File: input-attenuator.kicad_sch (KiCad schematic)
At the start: 44 parts, among them J1 DC_INTF, J2 RF_IN, J3 RX_1_RF, J4 RX_2_RF, K1 EE2-5TNU-L, K2 EE2-5TNU-L, K3 EE2-5TNU-L, K4 EE2-5TNU-L, Q1 MMBT3904, Q2 MMBT3904, Q3 MMBT3904, Q4 MMBT3904, Q5 MMBT3904, Q6 MMBT3904, Q7 MMBT3904, Q8 MMBT3904, U1 74HC595

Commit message: noComment
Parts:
- added C? (x4): 0.22u, Capacitor_SMD:C_0805_2012Metric, symbol Device:C_Small
- added C?: 100u, Capacitor_SMD:CP_Elec_6.3x5.4_Nichicon, symbol Device:CP_Small
- added D? (x6): 1N4148WS, Diode_SMD:D_SOD-323, symbol Device:D_Small_ALT
- added J?: DC_INTF, Connector_PinHeader_2.54mm:PinHeader_1x06_P2.54mm_Vertical, symbol Connector:Conn_01x06_Male
- added K? (x3): EE2-5TNU-L, Relay_SMD:Relay_DPDT_Kemet_EE2_NU_DoubleCoil, symbol Relay:EE2-5TNU
- added Q? (x8): BC858, Package_TO_SOT_SMD:SOT-23, symbol Transistor_BJT:BC858
- added R22, R23, R24, R? (x6): _, Resistor_SMD:R_0805_2012Metric, symbol Device:R_Small_US
- added R? (x7): 22K, Resistor_SMD:R_0805_2012Metric, symbol Device:R_Small_US
- added R? (x4): 1M, Resistor_SMD:R_0805_2012Metric, symbol Device:R_Small_US
- added R? (x2): 82.2, Resistor_SMD:R_0805_2012Metric, symbol Device:R_Small_US
- added R? (x4): 14.0_, Resistor_SMD:R_0805_2012Metric, symbol Device:R_Small_US
- added U1 (x4), U? (x16): 74HC00, symbol 74xx:74HC00
- R2, R3: value 14.0 -> 14.0_
- R4: value 82.2 -> 82.2
- renumbered U1 to U?
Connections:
- net A1_OFF: no longer R5.1
- net A1_ON: no longer R1.1
- net A2_ON: no longer R6.1
- net GND: now also D1.2 (A), D2.2 (A), K1.1, K1.6, C?.2, C?.2, C?.2, C?.2, C?.2, D?.2 (A), D?.2 (A), D?.2 (A), D?.2 (A), D?.2 (A), D?.2 (A), J?.2 (Pin_2), K?.1, K?.1, K?.1, K?.6, K?.6, K?.6, R24.2, R?.1, R?.2, R?.2, R?.2, R?.2; no longer Q1.2 (E), Q2.2 (E)
- net RF_IN: now also K?.4, K?.4
- net RX_2_RF: no longer J4.1 (In)
- net VRelay: now also C?.1, J?.1 (Pin_1), Q?.2 (E), Q?.2 (E), Q?.2 (E), Q?.2 (E), Q?.2 (E), Q?.2 (E), Q?.2 (E), Q?.2 (E); no longer D1.1 (K), D2.1 (K), D8.1 (K), K1.1, K1.6, K4.6
- net at K1.5, R3.1: now also R23.1
- net at K1.8, R2.2: now also R22.1
- net at K1.9: now also K?.4; no longer K2.4
- net at Q1.1 (B): no longer R1.2
- net at R5.2: now also Q?.1 (B); no longer Q2.1 (B)
- net at R2.1, R3.2, R4.1: now also R22.2, R23.2, R24.1
- net at K4.3, K4.8: no longer K3.9
- new net: D2.1 (K), K1.12, Q?.3 (C)
- new net: D1.1 (K), K1.7, Q?.3 (C)
- new net: R1.1, U1.3
- new net: Q?.1 (B), R1.2
- new net: R5.1, U1.3
- new net: D8.1 (K), K4.6
- new net: R?.1, U?.3 (x6)
- new net: Q?.1 (B), R?.2 (x6)
- new net: D?.1 (K), K?.7, Q?.3 (C) (x3)
- new net: R?.1, U1.1, U1.1, U1.2, U?.3
- new net: U1.1, U1.3
- new net: C?.1, R?.2, U1.1, U1.2, U1.2
- new net: U?.1, U?.3 (x3)
- new net: C?.1, R?.2, U?.1, U?.2, U?.2 (x3)
- new net: R?.1, U?.1, U?.1, U?.2, U?.3 (x3)
- new net: U?.2, U?.3 (x3)
- new net: K?.5, R?.1, R?.1 (x2)
- new net: R?.1, R?.1, R?.1, R?.2, R?.2, R?.2 (x2)
- new net: D?.1 (K), K?.12, Q?.3 (C) (x3)
- new net: U1.2, U1.3
- new net: K?.10, K?.3 (x2)
- new net: K?.8, R?.1, R?.2 (x2)
- new net 10dB: U?.1
- new net 20dB: U?.1
- new net 5dB: J?.3 (Pin_3), U?.1
- new net Rx: U?.1
- new net powerDown: R?.2, U?.2, U?.2, U?.2, U?.2
- now unconnected: Q1.3 (C), Q2.3 (C)
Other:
- note removed: "Receiver selector"
- moved on the sheet: C1, C2, D1, D2, D3, D4, D5, D6, D7, D8, J1, J2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

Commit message: relays
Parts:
- removed J2: RF_IN, Connector_Coaxial:SMA_Amphenol_132134_Vertical, symbol Connector:Conn_Coaxial
- removed Q? (x3): BC858, Package_TO_SOT_SMD:SOT-23, symbol Transistor_BJT:BC858
- removed R? (x3): 22K, Resistor_SMD:R_0805_2012Metric, symbol Device:R_Small_US
- added J?: RF_IN, Connector_Coaxial:SMA_Amphenol_132134_Vertical, symbol Connector:Conn_Coaxial
- added Q? (x3): BC858, Package_TO_SOT_SMD:SOT-23, symbol Transistor_BJT:BC858
- added R? (x3): 22K, Resistor_SMD:R_0805_2012Metric, symbol Device:R_Small_US
- added unit 5 of U1
- gave numbers to parts that had none: 3
- renumbered R5 to R2, R3 to R4, R23 to R5, R4 to R6, R24 to R7, R2 to R8, R22 to R9
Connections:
- net GND: now also J?.2 (Ext)
- net RX_1_RF: no longer J3.1 (In)
- net VRelay: now also Q?.2 (E), Q?.2 (E), Q?.2 (E)
- net at R1.1: now also U1.8; no longer U1.3
- net at R2.1: now also U1.11; no longer U1.3
- net Antenna: now reaches J4.1 (In)
- net Antenna: now also K?.4, K?.9
- net at R3.1, U1.1, U1.2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: now also U1.9; no longer U1.1
- net at U1.3: now also U1.12; no longer U1.1
- net at U?.3: now also R?.1 (x3)
- net at D?.1 (K), K?.12: now also Q?.3 (C) (x3)
- net RF_RX: now reaches K?.9
- net RF_RX: now also J3.1 (In)
- net RF_TX: now reaches K?.10
- net RF_TX: now also K?.3, J?.1 (In)
- net at K?.8: now also K1.4
- net at K?.9: now also K?.4
- removed net RF_IN: K1.4, K?.4, K?.4
- new net: C?.1, R3.2, U1.13, U1.4, U1.5
- new net: U1.10, U1.6
- new net: Q?.1 (B), R?.2 (x3)
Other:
- moved on the sheet: C?, D1, D2, D?, J3, J4, K1, K?, Q1, Q2, Q?, R1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

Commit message: relaysPlaced
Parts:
- removed C?: 100u, Capacitor_SMD:CP_Elec_6.3x5.4_Nichicon, symbol Device:CP_Small
- removed D3, D4, D5, D6, D7, D8: 1N4148WS, Diode_SMD:D_SOD-323, symbol Device:D_Small_ALT
- removed J?: DC_INTF, Connector_PinHeader_2.54mm:PinHeader_1x06_P2.54mm_Vertical, symbol Connector:Conn_01x06_Male
- removed K2, K3, K4: EE2-5TNU-L, Relay_SMD:Relay_DPDT_Kemet_EE2_NU_DoubleCoil, symbol Relay:EE2-5TNU
- removed Q2, Q3, Q4, Q5, Q6, Q7, Q8: MMBT3904, Package_TO_SOT_SMD:SOT-23, symbol Transistor_BJT:MMBT3904
- removed R10, R11, R15, R16, R17, R6, R?: 22K, Resistor_SMD:R_0805_2012Metric, symbol Device:R_Small_US
- removed R12, R13: 40.9, Resistor_SMD:R_0805_2012Metric, symbol Device:R_Small_US
- removed R14: 10.1, Resistor_SMD:R_0805_2012Metric, symbol Device:R_Small_US
- removed R7, R8: 26.0, Resistor_SMD:R_0805_2012Metric, symbol Device:R_Small_US
- removed R9: 35.1, Resistor_SMD:R_0805_2012Metric, symbol Device:R_Small_US
- added unit 5 of U2
- added unit 5 of U3
- added unit 5 of U4
- added unit 5 of U5
- U1: footprint (none) -> Package_SO:SO-14_3.9x8.65mm_P1.27mm
- U2, U3, U4, U5: renamed from U?; footprint (none) -> Package_SO:SO-14_3.9x8.65mm_P1.27mm
- gave numbers to parts that had none: 42
- renumbered Q1 to Q3
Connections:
- net A1_OFF is gone; now on net 5dB: U6.1 (QB)
- net A1_ON is gone; now on net Rx: U6.15 (QA)
- net A2_OFF is gone; now on net 20dB: U6.3 (QD)
- net A2_ON is gone; now on net 10dB: U6.2 (QC)
- net VRelay is gone; now on net +5V: C1.1, C2.2, J1.1 (Pin_1), Q1.2 (E), Q2.2 (E), Q4.2 (E), Q5.2 (E), Q6.2 (E), Q7.2 (E), Q8.2 (E), Q9.2 (E), U6.10 (~SRCLR), U6.16 (VCC)
- net 10dB: now also U5.9; no longer U5.1
- net 20dB: now also U5.13; no longer U5.1
- net 5dB: now also U5.5; no longer U5.1
- net GND: now also U1.7 (GND), U2.7 (GND), U3.7 (GND), U4.7 (GND), U5.7 (GND)
- net powerDown: now also U5.10, U5.12, U5.4; no longer U5.2, U5.2, U5.2
- net at K1.4, K2.8: now also K2.5
- net at R2.1: now also U1.6; no longer U1.11
- net at R27.1: now also U3.6; no longer U3.3
- net at R3.1, U1.1, U1.2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: now also U5.6; no longer U5.3
- net at U1.3: now also U1.4; no longer U1.12
- net at U2.3: now also U2.4; no longer U2.1
- net at R25.1: now also U2.6; no longer U2.3
- net at R30.1, U3.1, U3.2: now also U3.9, U5.11; no longer U3.1, U5.3
- net at R28.1, U4.1, U4.2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: now also U4.9; no longer U4.1
- net at R26.1: now also U3.8; no longer U3.3
- net at U1.10: now also U1.11; no longer U1.6
- net at R22.1: now also U4.8; no longer U4.3
- net +5V: now reaches U1.14 (VCC)
- net +5V: now also U2.14 (VCC), U3.14 (VCC), U4.14 (VCC), U5.14 (VCC)
- net at R29.1, U2.1, U2.2: now also U2.9, U5.8; no longer U2.1, U5.3
- net at R23.1: now also U4.6; no longer U4.3
- net at R24.1: now also U2.8; no longer U2.3
- net at U3.3: now also U3.4; no longer U3.1
- net at U4.3: now also U4.4; no longer U4.1
- net A3_OFF: no longer names the net of U6.5 (QF)
- net A3_ON: no longer names the net of U6.4 (QE)
- net RX_1_ON: no longer names the net of U6.6 (QG)
- net RX_2_ON: no longer names the net of U6.7 (QH)
- new net: C4.1, R3.2, U1.12, U1.13, U1.5
- new net: C5.1, R29.2, U2.12, U2.13, U2.5
- new net: C6.1, R30.2, U3.12, U3.13, U3.5
- new net: U3.10, U3.11
- new net: U4.10, U4.11
- new net: U2.10, U2.11
- new net: C3.1, R28.2, U4.12, U4.13, U4.5
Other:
- note removed: "Keep DRC happy"
- moved on the sheet: C1, C2, J1, Q3, U1E, U6

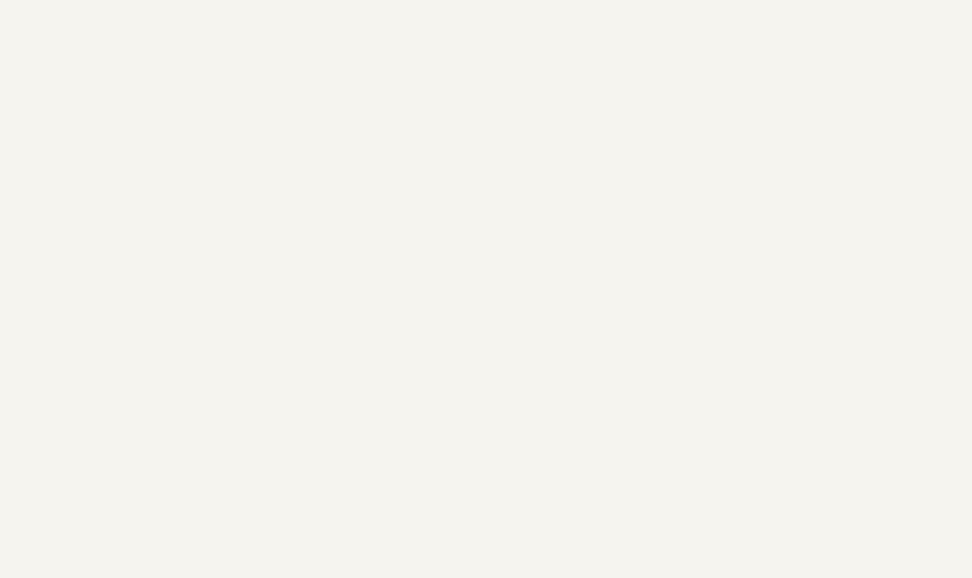
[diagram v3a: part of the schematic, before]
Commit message: Added regulator symbol to custom lib
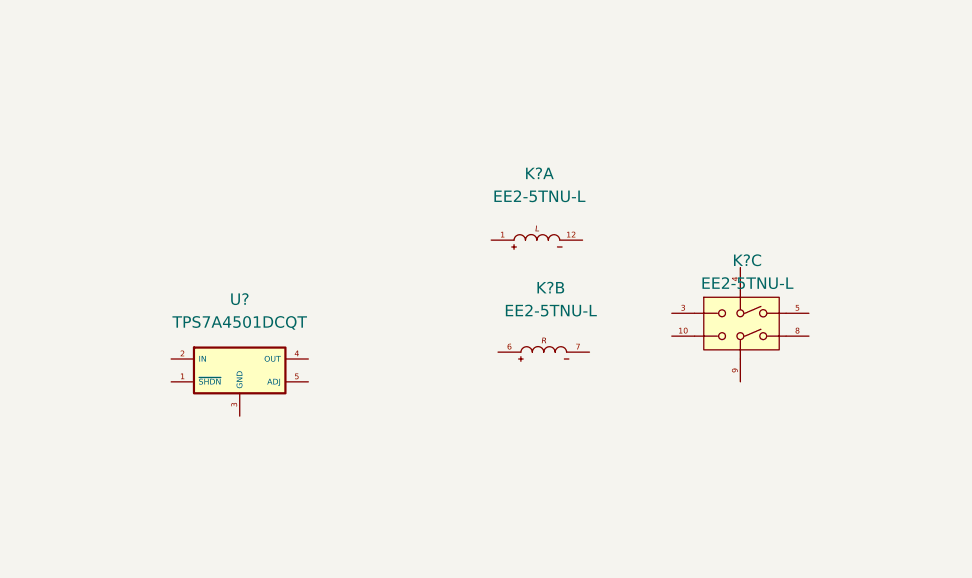
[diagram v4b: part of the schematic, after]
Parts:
- added K? (x3): EE2-5TNU-L, Relay_SMD:Relay_DPDT_Kemet_EE2_NU_DoubleCoil, symbol rf-designers:EE2-5TNU-L
- added U?: TPS7A4501DCQT, Package_TO_SOT_SMD:SOT-223-6, symbol rf-designers:TPS7A4501DCQT
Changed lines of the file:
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@@
     (pin "2")
+  )
+  (symbol (lib_id "rf-designers:EE2-5TNU-L") (at 224.79 132.588 0) (unit 1)
+    (in_bom yes) (on_board yes)
+    (property "Reference" "K?" (id 0) (at 225.044 125.222 0))
+    (property "Value" "EE2-5TNU-L" (id 1) (at 225.044 127.762 0))
+    (property "Footprint" "Relay_SMD:Relay_DPDT_Kemet_EE2_NU_DoubleCoil" (id 2) (at 228.6 114.808 0)
+      (effects (font (size 1.27 1.27)) hide)
+    )
+    (property "Datasheet" "" (id 3) (at 228.6 114.808 0)
+      (effects (font (size 1.27 1.27)) hide)
+    )
+    (pin "1")
+    (pin "12")
+  )
+  (symbol (lib_id "rf-designers:EE2-5TNU-L") (at 225.552 145.034 0) (unit 2)
+    (in_bom yes) (on_board yes)
+    (property "Reference" "K?" (id 0) (at 226.314 137.922 0))
+    (property "Value" "EE2-5TNU-L" (id 1) (at 226.314 140.462 0))
+    (property "Footprint" "Relay_SMD:Relay_DPDT_Kemet_EE2_NU_DoubleCoil" (id 2) (at 229.362 127.254 0)
+      (effects (font (size 1.27 1.27)) hide)
+    )
+    (property "Datasheet" "" (id 3) (at 229.362 127.254 0)
+      (effects (font (size 1.27 1.27)) hide)
+    )
+    (pin "6")
+    (pin "7")
   )
   (symbol (lib_id "Connector:Conn_Coaxial") (at 19.685 32.385 0) (mirror y) (unit 1)
@@
     (pin "5")
     (pin "6")
+  )
+  (symbol (lib_id "rf-designers:TPS7A4501DCQT") (at 191.77 145.796 0) (unit 1)
+    (in_bom yes) (on_board yes)
+    (property "Reference" "U?" (id 0) (at 191.77 139.192 0))
+    (property "Value" "TPS7A4501DCQT" (id 1) (at 191.77 141.732 0))
+    (property "Footprint" "Package_TO_SOT_SMD:SOT-223-6" (id 2) (at 191.77 135.636 0)
+      (effects (font (size 1.27 1.27)) hide)
+    )
+    (property "Datasheet" "http://www.ti.com/lit/ds/symlink/tps7a45.pdf" (id 3) (at 185.42 147.066 0)
+      (effects (font (size 1.27 1.27)) hide)
+    )
+    (pin "1")
+    (pin "2")
+    (pin "3")
+    (pin "4")
+    (pin "5")
+  )
+  (symbol (lib_id "rf-designers:EE2-5TNU-L") (at 247.65 141.732 0) (unit 3)
+    (in_bom yes) (on_board yes)
+    (property "Reference" "K?" (id 0) (at 248.158 134.874 0))
+    (property "Value" "EE2-5TNU-L" (id 1) (at 248.158 137.414 0))
+    (property "Footprint" "Relay_SMD:Relay_DPDT_Kemet_EE2_NU_DoubleCoil" (id 2) (at 251.46 123.952 0)
+      (effects (font (size 1.27 1.27)) hide)
+    )
+    (property "Datasheet" "" (id 3) (at 251.46 123.952 0)
+      (effects (font (size 1.27 1.27)) hide)
+    )
+    (pin "10")
+    (pin "3")
+    (pin "4")
+    (pin "5")
+    (pin "8")
+    (pin "9")
   )
   (symbol (lib_id "74xx:74HC00") (at 90.805 172.72 0) (unit 5)
@@
       (reference "K4") (unit 1) (value "EE2-5TNU-L") (footprint "Relay_SMD:Relay_DPDT_Kemet_EE2_NU_DoubleCoil")
     )
+    (path "/3e6b9cc2-ca34-441f-a166-9b3684d3e6d6"
+      (reference "K?") (unit 1) (value "EE2-5TNU-L") (footprint "Relay_SMD:Relay_DPDT_Kemet_EE2_NU_DoubleCoil")
+    )
+    (path "/1bb0ed99-a77d-425c-9aa7-9bfc6da51c12"
+      (reference "K?") (unit 2) (value "EE2-5TNU-L") (footprint "Relay_SMD:Relay_DPDT_Kemet_EE2_NU_DoubleCoil")
+    )
+    (path "/6cacef75-4a83-4fd3-9cdf-800ba8a8ad1b"
+      (reference "K?") (unit 3) (value "EE2-5TNU-L") (footprint "Relay_SMD:Relay_DPDT_Kemet_EE2_NU_DoubleCoil")
+    )
     (path "/5cabdd49-e7e5-41d2-b7d5-019de18d0b22"
       (reference "Q1") (unit 1) (value "BC858") (footprint "Package_TO_SOT_SMD:SOT-23")
@@
       (reference "U6") (unit 1) (value "74HC595") (footprint "Package_SO:SO-16_5.3x10.2mm_P1.27mm")
     )
-  )
+    (path "/8354ecd4-2a4f-44f8-a737-ff9cdb5f7927"
+      (reference "U?") (unit 1) (value "TPS7A4501DCQT") (footprint "Package_TO_SOT_SMD:SOT-223-6")
+    )
+  )

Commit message: addedPowerDown
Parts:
- added C?: 0.22u, Capacitor_SMD:C_0805_2012Metric, symbol Device:C_Small
- added D?: 1N4148WS, Diode_SMD:D_SOD-323, symbol Device:D_Small_ALT
- added D?: WRONG DIODE, Diode_SMD:D_SOD-323, symbol Device:D_Small_ALT
- added Q?: MMBT3904, Package_TO_SOT_SMD:SOT-23, symbol Transistor_BJT:MMBT3904
- added R?: 180k, Resistor_SMD:R_0805_2012Metric, symbol Device:R_Small_US
- added R? (x9): 1M, Resistor_SMD:R_0805_2012Metric, symbol Device:R_Small_US
- added R?: 220k, Resistor_SMD:R_0805_2012Metric, symbol Device:R_Small_US
- added R?: 3M3, Resistor_SMD:R_0805_2012Metric, symbol Device:R_Small_US
- added R?: 470k, Resistor_SMD:R_0805_2012Metric, symbol Device:R_Small_US
- added R?: 100k, Resistor_SMD:R_0805_2012Metric, symbol Device:R_Small_US
- added U? (x3): LP339, symbol Comparator:LM339
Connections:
- net powerDown is gone; now on net PowerDn: U5.10, U5.12, U5.2, U5.4
- net +5V: now also U?.4 (OUT), R?.2, R?.2, U?.4 (-), U?.4 (-); no longer C1.1, J1.1 (Pin_1)
- net GND: now also Q3.2 (E), U?.3 (GND), C?.2, Q?.2 (E), R?.1, R?.1, R?.1, R?.2, R?.2, U?.12 (V-)
- net at Q3.1 (B): now also Q?.3 (C), R?.1
- net PowerDn: now reaches Q3.3 (C)
- net PowerDn: now also R?.1, U?.2
- net at U?.1 (~SHDN): now also C?.1, D?.1 (K), R?.2
- net Vin2: now reaches U?.2 (IN)
- net Vin2: now also C1.1, D?.1 (K), R?.2, R?.2, R?.2, U?.3 (V+)
- net at U?.5 (ADJ): now also R?.1, R?.2
- new net: R?.1, R?.1, U?.2, U?.5 (+)
- new net: Q?.1 (B), R?.1, R?.1
- new net: R?.1, R?.2, R?.2, U?.5 (+)
- new net +2V5: R?.1, R?.1
- new net SHDN: D?.2 (A), R?.2
- new net Vin: D?.2 (A), J1.1 (Pin_1), R?.2
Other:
- note added: "Need xtra pin for SHDN Need correct Vin diode"
- note added: "SHDN will reset relays and later shut down power Low Vin will reset relays but not shut down power. In latter case we need 5V as a reference."
- moved on the sheet: C1, K?A, K?B, K?C, Q3, U?
